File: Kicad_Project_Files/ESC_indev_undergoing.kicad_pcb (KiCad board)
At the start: 2 copper layers, 64.5 x 76.5 mm, 64 parts, among them J2 JST_PH_1x04_P2mm, J3 JST_PH_1x04_P2mm, Q1 NMOS, Q2 NMOS, Q3 NMOS, Q4 NMOS, Q5 NMOS, Q6 NMOS, SW1 SW_Push, SW2 SW_Push, U1 TPS560430X3FDBVR, U11 LMV324, U2 IR2110S, U3 IR2110S, U4 IR2110S, U5 ESP32-WROOM-32E

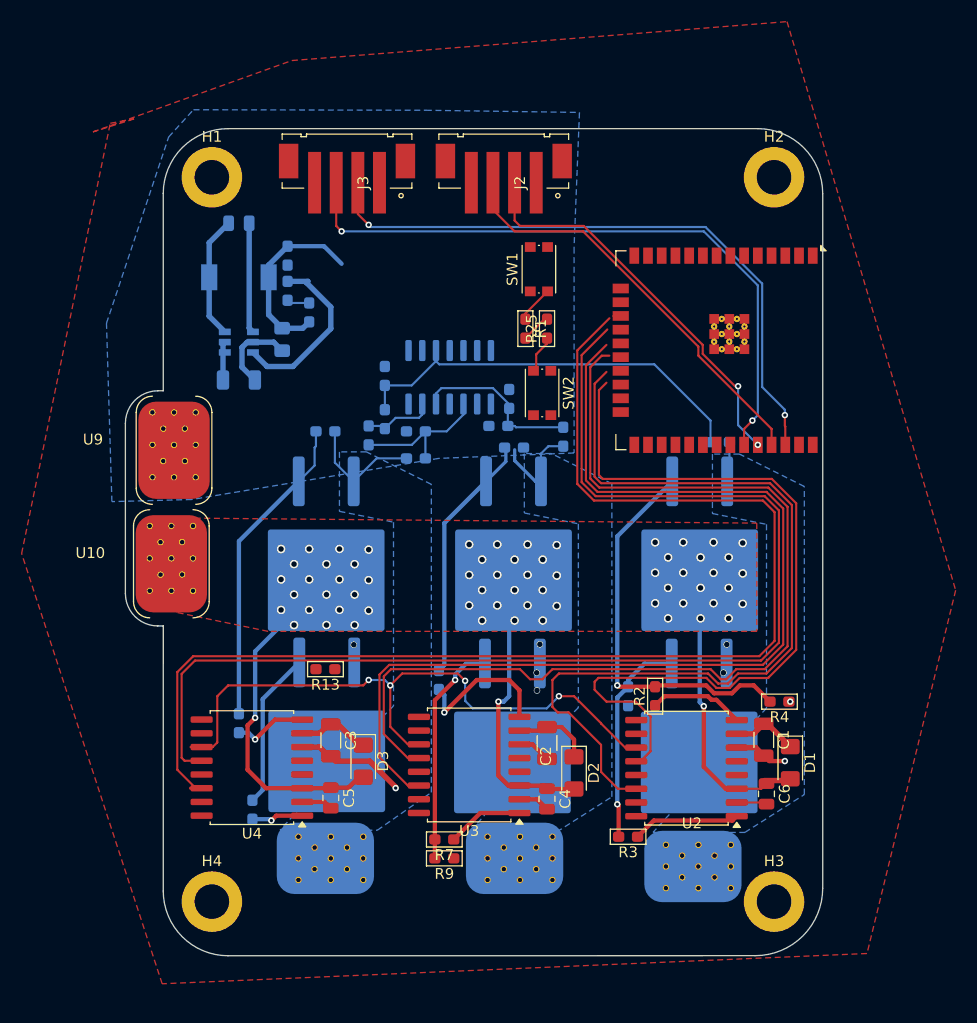
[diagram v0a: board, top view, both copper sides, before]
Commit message: major updates
updated GPIO assignments along with some component orientation , also changed the dimensions to fit everything in
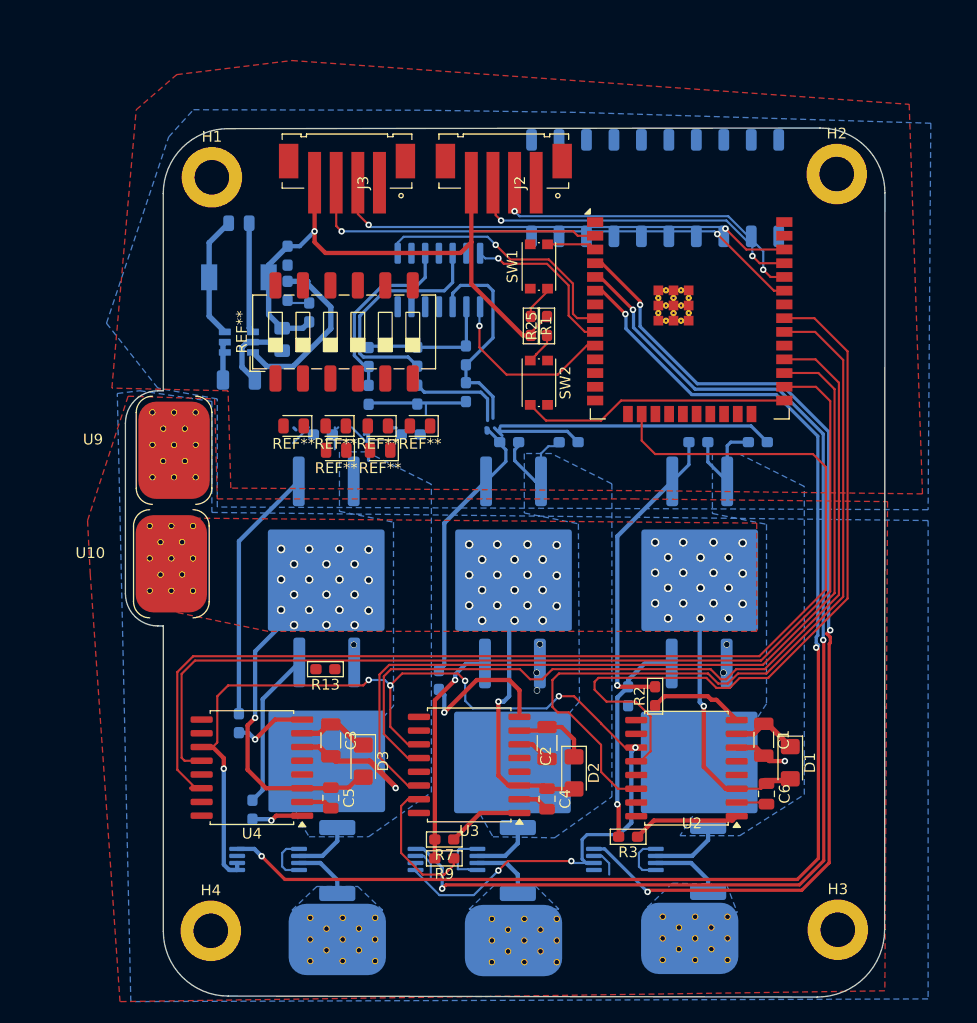
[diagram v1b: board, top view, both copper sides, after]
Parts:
- added R26: R_US, Resistor_SMD:R_2512_6332Metric_Pad1.40x3.35mm_HandSolder, B.Cu at (244.9, 97.1)
- added R27: R_US, Resistor_SMD:R_2512_6332Metric_Pad1.40x3.35mm_HandSolder, B.Cu at (227.3, 97.2)
- added R28: R_US, Resistor_SMD:R_2512_6332Metric_Pad1.40x3.35mm_HandSolder, B.Cu at (210.6, 97.2)
- added REF**: LED_0805_2012Metric, LED_SMD:LED_0805_2012Metric, F.Cu at (214.4, 57.0)
- added REF**: LED_0805_2012Metric, LED_SMD:LED_0805_2012Metric, F.Cu at (206.6, 57.0)
- added REF**: LED_0805_2012Metric, LED_SMD:LED_0805_2012Metric, F.Cu at (214.6, 59.2)
- added REF**: SW_DIP_SPSTx06_Slide_6.7x16.8mm_W8.61mm_P2.54mm_LowProfile, Button_Switch_SMD:SW_DIP_SPSTx06_Slide_6.7x16.8mm_W8.61mm_P2.54mm_LowProfile, F.Cu at (211.2, 48.3)
- added REF**: LED_0805_2012Metric, LED_SMD:LED_0805_2012Metric, F.Cu at (210.5, 59.2)
- added REF**: LED_0805_2012Metric, LED_SMD:LED_0805_2012Metric, F.Cu at (210.5, 57.0)
- added REF**: LED_0805_2012Metric, LED_SMD:LED_0805_2012Metric, F.Cu at (218.2, 57.0)
- added REF**: 2x10_SMD_Horizontal, PCM_SparkFun-Connector:2x10_P2.54mm_Socket_Horizontal_SMD, B.Cu at (240.0, 35.0)
- added U15: INA240A1PW, Package_SO:TSSOP-8_4.4x3mm_P0.65mm, B.Cu at (237.2, 97.1)
- added U16: INA240A1PW, Package_SO:TSSOP-8_4.4x3mm_P0.65mm, B.Cu at (220.7, 97.1)
- added U17: INA240A1PW, Package_SO:TSSOP-8_4.4x3mm_P0.65mm, B.Cu at (204.2, 97.1)
- R4: moved to B.Cu
- moved R4 25.1 mm to (244.0, 58.5)
- moved R21 9.86 mm to (218.0, 50.6), turned to 90 degrees
- moved R16 9.54 mm to (222.5, 50.5), turned to 90 degrees
- moved U11 9.06 mm to (220.0, 43.5), turned to -90 degrees
- moved U5 9.00 mm to (243.2, 43.4), turned to 0 degrees
- moved R20 8.51 mm to (218.0, 54.1), turned to 90 degrees
- moved R18 7.65 mm to (222.5, 53.9), turned to 90 degrees
- moved U7 7.61 mm to (227.9, 112.1)
- moved U6 7.58 mm to (211.1, 112.0)
- moved R24 7.25 mm to (213.5, 50.6)
- moved U8 6.66 mm to (243.7, 111.9)
- moved H3 6.45 mm to (256.9, 103.6)
- moved H2 5.81 mm to (256.8, 33.7)
- moved R23 5.53 mm to (213.5, 54.1), turned to 90 degrees
- moved R17 3.50 mm to (249.5, 58.5), turned to 180 degrees
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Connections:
- U10 pad 1: (no net) -> /15v
- U11 pad 1: Net-(U5-IO26) -> Bemf1
- U11 pad 7: Net-(U5-IO27) -> Bemf2
- U11 pad 8: Net-(U5-IO32) -> Bemf3
- U5 pad 10: /HIN1 -> Bemf3
- U5 pad 11: Net-(U5-IO26) -> unconnected-(U5-IO26-Pad11)
- U5 pad 12: Net-(U5-IO27) -> unconnected-(U5-IO27-Pad12)
- U5 pad 16: unconnected-(U5-IO13-Pad16) -> /LIN3
- U5 pad 26: unconnected-(U5-IO4-Pad26) -> /HIN3
- U5 pad 27: unconnected-(U5-IO16-Pad27) -> /LIN2
- U5 pad 28: unconnected-(U5-IO17-Pad28) -> /HIN2
- U5 pad 30: unconnected-(U5-IO18-Pad30) -> /LIN1
- U5 pad 31: unconnected-(U5-IO19-Pad31) -> /HIN1
- U5 pad 4: unconnected-(U5-SENSOR_VP-Pad4) -> Isen1
- U5 pad 5: unconnected-(U5-SENSOR_VN-Pad5) -> Isen2
- U5 pad 6: unconnected-(U5-IO34-Pad6) -> Isen3
- U5 pad 8: Net-(U5-IO32) -> Bemf1
- U5 pad 9: unconnected-(U5-IO33-Pad9) -> Bemf2
- U9 pad 2: (no net) -> GND
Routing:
- net Isen3: track 0.00 -> 122.2 mm, vias 0 -> 3
- net Isen2: track 0.00 -> 109.0 mm, vias 0 -> 3
- net Isen1: track 0.00 -> 94.2 mm, vias 0 -> 3
- net +3.3V: track 78.9 -> 172.6 mm, vias 4 -> 9
- net GND: track 18.5 -> 62.0 mm
- net Net-(U11B-+): track 15.8 -> 41.8 mm
- net Net-(U5-IO0): track 3.54 -> 27.8 mm
- net Bemf1: track 0.00 -> 24.2 mm, vias 0 -> 1
- net /HIN3: track 112.8 -> 95.3 mm
- net Bemf3: track 0.00 -> 16.6 mm, vias 0 -> 1
- net Bemf2: track 0.00 -> 15.3 mm, vias 0 -> 1
- net Net-(U5-IO22): track 58.8 -> 43.7 mm
- net /LIN2: track 96.1 -> 81.7 mm
- net Net-(U5-IO21): track 60.6 -> 47.9 mm
- net /HIN2: track 94.3 -> 81.8 mm
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- added copper zone on B.Cu, net /PR1
- added copper zone on B.Cu, net /PR2
- added copper zone on B.Cu, net /PR3
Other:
- board size 64.5 x 76.5 mm -> 70.3 x 80.4 mm

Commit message: updated schematic with comp values
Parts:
- removed REF** (x6): LED_0805_2012Metric, LED_SMD:LED_0805_2012Metric
- removed REF**: SW_DIP_SPSTx06_Slide_6.7x16.8mm_W8.61mm_P2.54mm_LowProfile, Button_Switch_SMD:SW_DIP_SPSTx06_Slide_6.7x16.8mm_W8.61mm_P2.54mm_LowProfile
- removed REF**: 2x10_SMD_Horizontal, PCM_SparkFun-Connector:2x10_P2.54mm_Socket_Horizontal_SMD
- removed U1: TPS560430X3FDBVR, Kicad_Project_Files:IC_TPS560430X3FDBVR
- added C10: 100nf, Capacitor_SMD:C_0805_2012Metric_Pad1.18x1.45mm_HandSolder, F.Cu at (198.0, 49.5)
- added D14: TMMBAT45, PCM_Diode_SMD_AKL:D_MiniMELF, F.Cu at (201.0, 45.0)
- added D15: TMMBAT45, PCM_Diode_SMD_AKL:D_MiniMELF, F.Cu at (201.0, 42.0)
- added D5: RED_LED, LED_SMD:LED_1206_3216Metric, F.Cu at (256.5, 39.0)
- added D6: GREEN_LED, LED_SMD:LED_1206_3216Metric, F.Cu at (256.5, 42.0)
- added D7: GREEN_LED, LED_SMD:LED_1206_3216Metric, F.Cu at (256.5, 45.0)
- added R29: 330ohm, PCM_Resistor_SMD_AKL:R_0805_2012Metric, B.Cu at (206.5, 52.5)
- added R30: 4.7k, PCM_Resistor_SMD_AKL:R_0805_2012Metric, F.Cu at (197.0, 46.0)
- added R32: 56k, PCM_Resistor_SMD_AKL:R_0805_2012Metric, F.Cu at (202.5, 49.5)
- added R33: R_US, PCM_Resistor_SMD_AKL:R_0603_1608Metric_Pad1.05x0.95mm_HandSolder, F.Cu at (257.0, 51.5)
- added R34: R_US, PCM_Resistor_SMD_AKL:R_0603_1608Metric_Pad1.05x0.95mm_HandSolder, F.Cu at (257.0, 49.5)
- added R35: R_US, PCM_Resistor_SMD_AKL:R_0603_1608Metric_Pad1.05x0.95mm_HandSolder, F.Cu at (257.0, 47.5)
- added SW3: SW_DIP_x04, Button_Switch_SMD:SW_DIP_SPSTx04_Slide_6.7x11.72mm_W8.61mm_P2.54mm_LowProfile, F.Cu at (211.0, 48.5)
- added U12: TPS54302, Package_TO_SOT_SMD:SOT-23-6, B.Cu at (201.0, 49.5)
- C1, C2: value C -> 1uf
- C3: value C -> iuf
- C7: value C -> 10uf
- C8: value C -> 0.1uf
- C9: value C -> 22uf
- D1, D2, D3: value 1N4001 -> uf4007
- L1: value L -> 6.8uH
- R1: value R_US -> 10k
- R10, R11, R2, R3, R6, R7: value R_US -> 22
- R14: value R_US -> 100k
- R15: value R_US -> 22k
- moved D4 2.55 mm to (208.5, 49.0)
- moved C8 2.02 mm to (199.5, 38.5), turned to 0 degrees
- moved R14 0.56 mm to (206.5, 41.5)
- moved R15 0.56 mm to (206.5, 44.8)
- moved C7 0.25 mm to (201.5, 52.5)
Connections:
- D4 pad 2: +3.3V -> Net-(D4-A)
- U5 pad 11: unconnected-(U5-IO26-Pad11) -> LED2
- U5 pad 13: unconnected-(U5-IO14-Pad13) -> LED1
- U5 pad 14: unconnected-(U5-IO12-Pad14) -> DIP1
- U5 pad 23: unconnected-(U5-IO15-Pad23) -> DIP2
- U5 pad 24: unconnected-(U5-IO2-Pad24) -> DIP3
- U5 pad 29: unconnected-(U5-IO5-Pad29) -> DIP4
- U5 pad 37: unconnected-(U5-IO23-Pad37) -> LED2
- U5 pad 7: unconnected-(U5-IO35-Pad7) -> DC sense
- U6 pad 2: (no net) -> /PR3
- U7 pad 2: (no net) -> /PR2
- U8 pad 2: (no net) -> /PR1
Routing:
- net +3.3V: track 172.6 -> 263.6 mm, vias 9 -> 10
- net DC sense: track 0.00 -> 53.1 mm, vias 0 -> 2
- net DIP2: track 0.00 -> 43.0 mm, vias 0 -> 2
- net DIP3: track 0.00 -> 42.1 mm, vias 0 -> 2
- net DIP4: track 0.00 -> 41.4 mm, vias 0 -> 2
- net DIP1: track 0.00 -> 30.8 mm
- net /15v: track 89.9 -> 120.2 mm, vias 66 -> 67
- net Net-(D5-A): track 0.00 -> 14.2 mm
- net Net-(U12-BOOT): track 10.2 -> 23.4 mm
- net Net-(U11A-+): track 17.6 -> 29.4 mm
- net Net-(D6-A): track 0.00 -> 8.89 mm
- net GND: track 62.0 -> 53.8 mm, vias 6 -> 12
- net Net-(D7-A): track 0.00 -> 4.26 mm
- net Net-(U12-FB): track 16.4 -> 20.3 mm
- net Net-(D4-A): track 0.00 -> 3.08 mm
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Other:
- board size 70.3 x 80.4 mm -> 71.2 x 80.4 mm
